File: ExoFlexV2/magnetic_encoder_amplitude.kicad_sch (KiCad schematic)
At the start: 29 parts, among them U11 ADCMP602BRMZ, U12 ADCMP602BRMZ, U13 ADCMP602BRMZ, U14 SN74LVC3G14DCUT_V2, U15 SN74LV4T08PWR_V2, U16 SN74HC7032D_V2, U4 SN74HC7032D_V2

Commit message: quque truc
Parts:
- added C20, C21, C22, C23, C24, C25: 1nF, Capacitor_SMD:C_0603_1608Metric, symbol Device:C
- added R11, R12, R14, R17, R18, R19: 7,5k, Resistor_SMD:R_0603_1608Metric, symbol Device:R_Small_US
- added R13: 150, Resistor_SMD:R_0603_1608Metric, symbol Device:R_Small_US
- added TP10, TP11, TP15, TP6, TP7, TP8, TP9: 5005, FootPrint:KEYSTONE_5005, symbol SymLib:5005
- R10, R8, R9: value R_Small_US -> 5k
- R15: renamed from R11; value R_Small_US -> 3,6k
- R16: renamed from R12; value R_Small_US -> 2,5k
- R7: value R_Small_US -> 2,5k
- renumbered C20 to C26, C21 to C27, C22 to C28, C23 to C29, C24 to C30, C25 to C31, C26 to C32, C27 to C33, C28 to C34, C29 to C35, C30 to C36, C31 to C37, C32 to C38, TP1 to TP12, TP2 to TP13, TP3 to TP14, U11 to U12, U12 to U13, U13 to U14, U14 to U15, U15 to U16, U16 to U17, U4 to U5
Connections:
- net +5V: no longer R15.1, R7.1, R9.1
- net +5VA: now also R7.1, R9.1, R13.1; no longer C26.2, C27.2, C28.2, C29.2, C30.2, C31.2, C32.2, C33.2, C34.2, C35.2, C36.2, C37.2, C38.2, R10.1, R16.1, R8.1, U12.6 (GND), U13.6 (GND), U14.6 (GND), U17.7 (GND)
- net MAG1_POT_OUT: now also R17.1; no longer U12.3 (VN)
- net MAG2_POT_OUT: now also R18.1; no longer U13.3 (VN)
- net MAG3_POT_OUT: now also R19.1; no longer U14.2 (VP), U14.3 (VN)
- net MAG_AMP_1: now also C22.1, R14.2, TP7.TP
- net MAG_AMP_2: now also C21.1, R12.2, TP9.TP
- net MAG_AMP_SEC: now also TP15.TP
- new net: R13.2, R15.1
- new net GND: C20.2, C21.2, C22.2, C23.2, C24.2, C25.2, C26.2, C27.2, C28.2, C29.2, C30.2, C31.2, C32.2, C33.2, C34.2, C35.2, C36.2, C37.2, C38.2, R10.1, R16.1, R8.1, U12.6 (GND), U13.6 (GND), U14.6 (GND), U17.7 (GND)
- new net MAG_AMP_3: C20.1, C25.1, R11.2, R19.2, TP11.TP, TP6.TP, U14.2 (VP), U14.3 (VN)
- new net MAG_LIM_1: C23.1, R17.2, TP8.TP, U12.3 (VN)
- new net MAG_LIM_2: C24.1, R18.2, TP10.TP, U13.3 (VN)
- new net MAG_OUT_1: R14.1
- new net MAG_OUT_2: R12.1
- new net MAG_OUT_3: R11.1
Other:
- moved on the sheet: R10, R15, R16, R7, R8, R9

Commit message: Placement
Début du placement et modification d'après dernier review
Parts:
- added TP29, TP30, TP31: 5005, FootPrint:KEYSTONE_5005, symbol SymLib:5005
- renumbered C22 to C20, C23 to C21, C21 to C22, C24 to C23, C20 to C24, R9 to R10, R10 to R11, R13 to R12, R15 to R13, R16 to R14, R14 to R15, R17 to R16, R12 to R17, R11 to R19, R19 to R20, R7 to R8, R8 to R9, TP7 to TP20, TP8 to TP21, TP9 to TP22, TP10 to TP23, TP6 to TP24, TP11 to TP25, TP12 to TP26, TP13 to TP27, TP14 to TP28, TP15 to TP32, U12 to U10, U13 to U11, U14 to U12, U15 to U13, U5 to U14, U16 to U15, U17 to U16
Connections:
- net MAG_AMP_3: no longer C25.1, R20.2, TP25.TP, U12.3 (VN)
- net at U14.11 (4Y), U16.1 (1A): now also TP30.TP
- net at U15.6 (2Y), U16.2 (1B): now also TP31.TP
- net at U13.5 (2Y), U15.4 (2A): now also TP29.TP
- new net MAG_LIM_3: C25.1, R20.2, TP25.TP, U12.3 (VN)
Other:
- moved on the sheet: C20, C22, C24, C25, R13, R14, R15, R17, R19, R20, TP24, TP26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

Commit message: Placement encore
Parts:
- renumbered C20 to C21, C21 to C22, C22 to C23, C23 to C24, C24 to C25, C25 to C26, C26 to C27, C27 to C28, C28 to C29, C29 to C30, C30 to C31, C31 to C32, C32 to C33, C33 to C34, C34 to C35, C35 to C36, C36 to C37, C37 to C38, C38 to C39, R9 to R10, R10 to R11, R11 to R12, R12 to R13, R13 to R14, R14 to R15, R15 to R16, R16 to R17, R17 to R18, R18 to R19, R19 to R20, R20 to R21, R8 to R9, U10 to U11, U11 to U12, U12 to U13, U13 to U14, U14 to U15, U15 to U16, U16 to U17

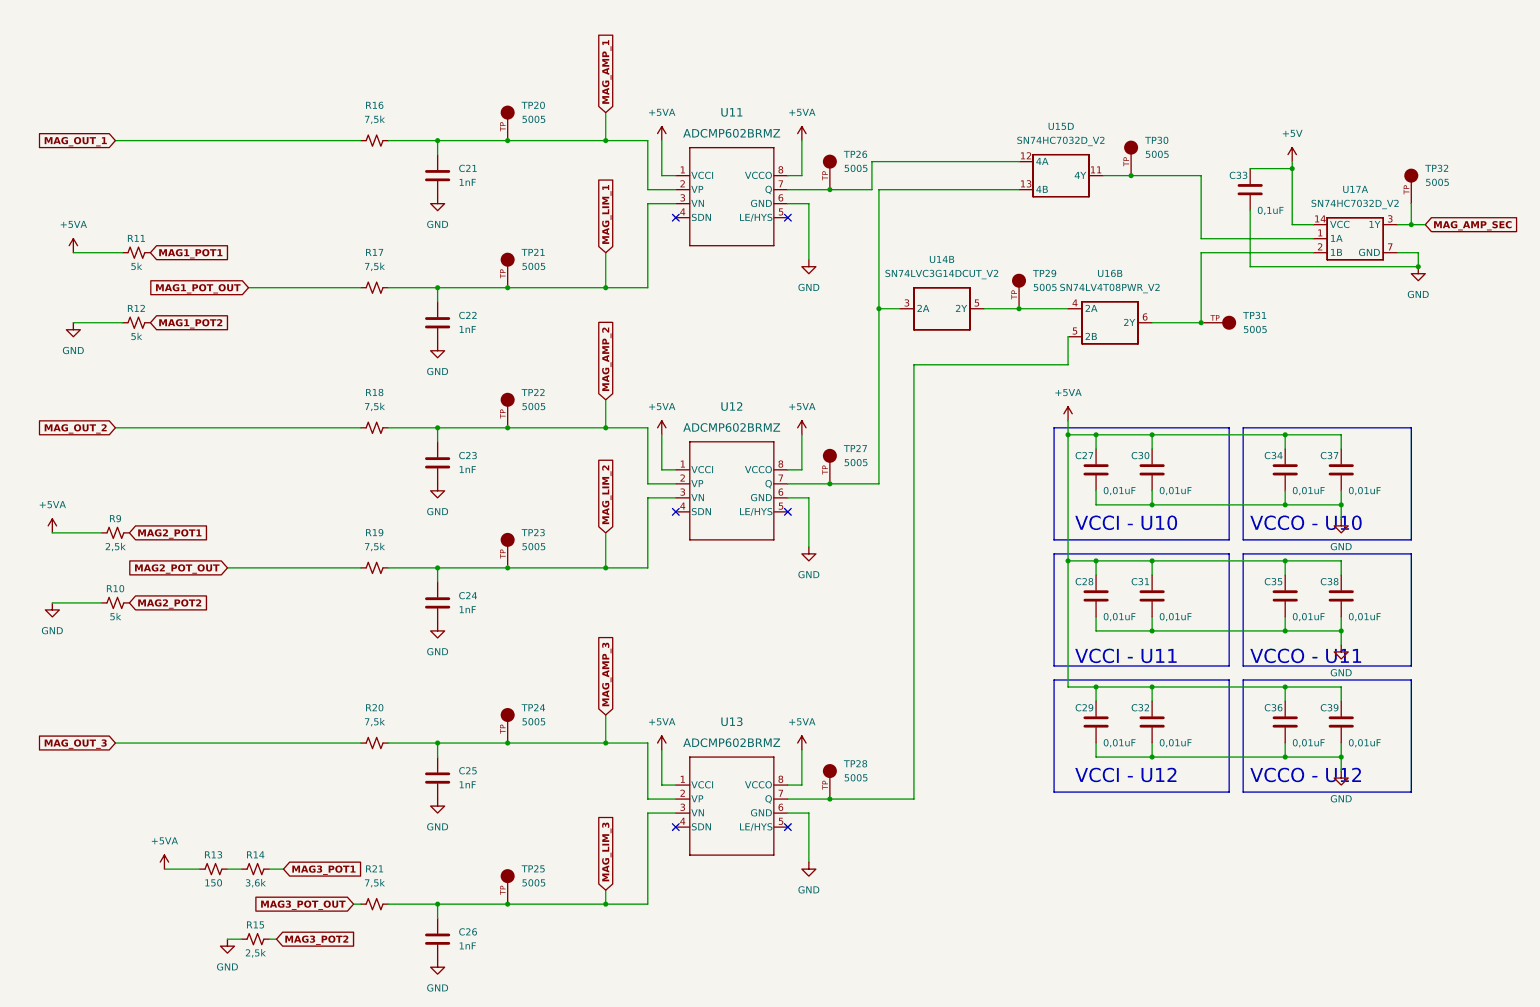
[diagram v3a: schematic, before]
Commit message: Mise à jour mi-stage
- Torque et Amplitude testé et vérifié
- Capteur de présence et de proximité testé
- Système de détection de coupure de fils
- Polyvalence pour plusieurs capteurs
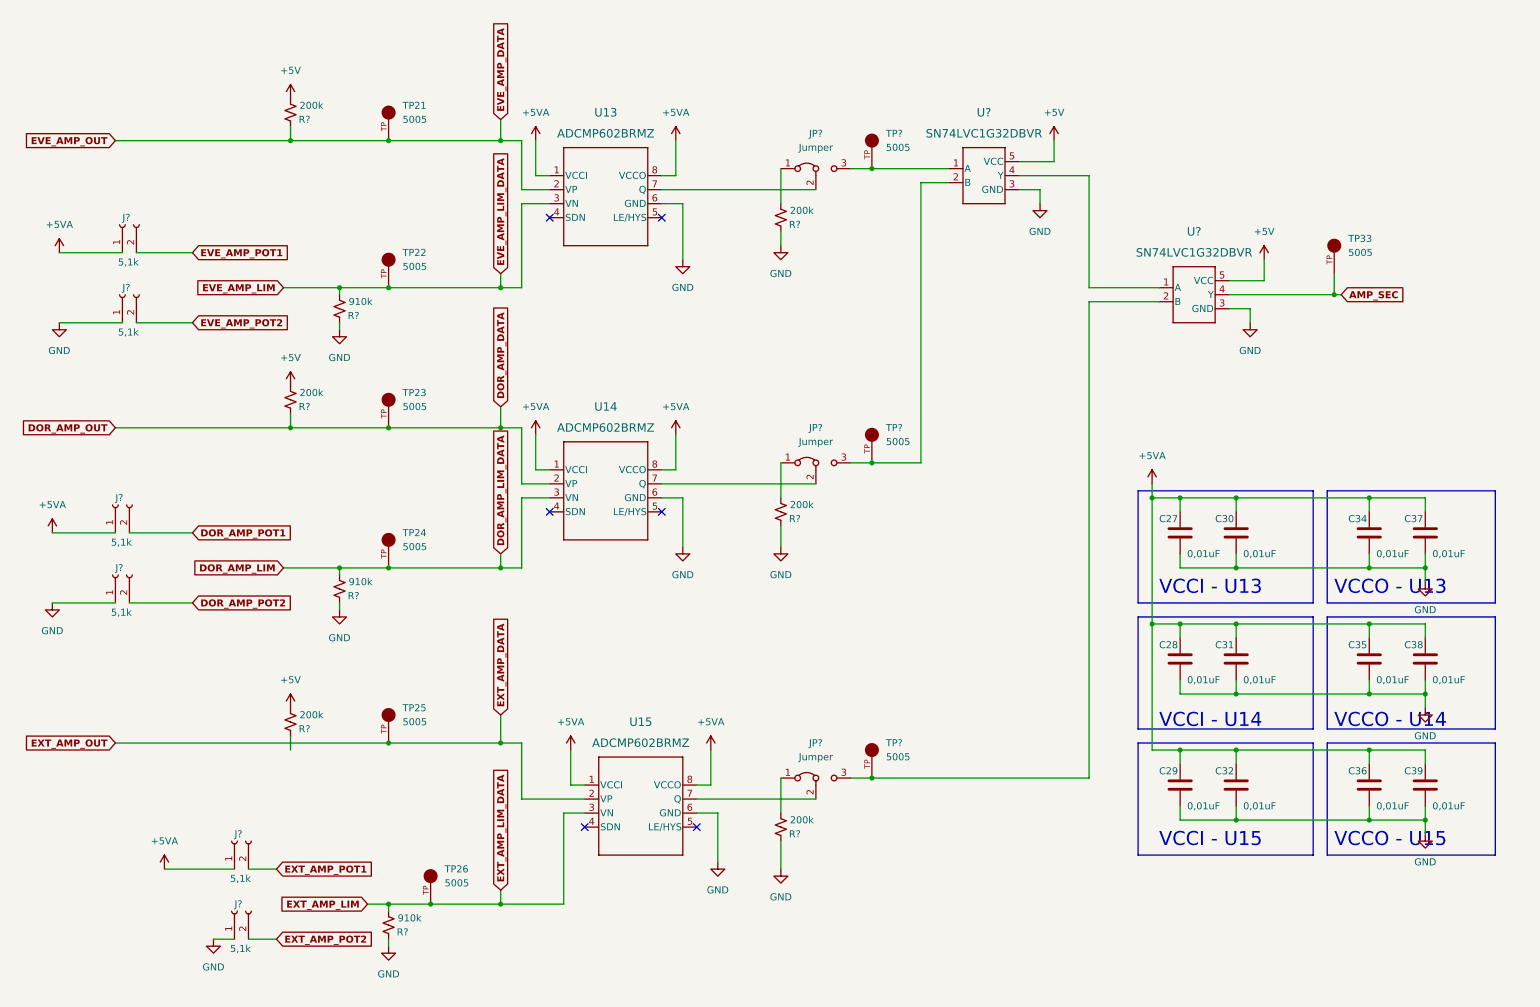
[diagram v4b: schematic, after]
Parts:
- removed C21, C22, C23, C24, C25, C26: 1nF, Capacitor_SMD:C_0603_1608Metric, symbol Device:C
- removed C33: 0,1uF, Capacitor_SMD:C_0603_1608Metric, symbol Device:C
- removed R10, R11, R12: 5k, Resistor_SMD:R_0603_1608Metric, symbol Device:R_Small_US
- removed R13: 150, Resistor_SMD:R_0603_1608Metric, symbol Device:R_Small_US
- removed R14: 3,6k, Resistor_SMD:R_0603_1608Metric, symbol Device:R_Small_US
- removed R15, R9: 2,5k, Resistor_SMD:R_0603_1608Metric, symbol Device:R_Small_US
- removed R16, R17, R18, R19, R20, R21: 7,5k, Resistor_SMD:R_0603_1608Metric, symbol Device:R_Small_US
- removed TP26, TP27, TP28, TP29, TP30, TP31: 5005, FootPrint:KEYSTONE_5005, symbol SymLib:5005
- removed U14: SN74LVC3G14DCUT_V2, FootPrint:SN74LVC3G14DCUT, symbol SymLib:SN74LVC3G14DCUT_V2
- removed U15, U17: SN74HC7032D_V2, FootPrint:SN74HC7032D, symbol SymLib:SN74HC7032D_V2
- removed U16: SN74LV4T08PWR_V2, FootPrint:SN74LV4T08PWR, symbol SymLib:SN74LV4T08PWR_V2
- added J? (x6): 5,1k, Connector_PinHeader_2.54mm:PinHeader_1x02_P2.54mm_Vertical, symbol Connector:Conn_01x02_Female
- added JP? (x3): Jumper, Connector_PinHeader_2.54mm:PinHeader_1x03_P2.54mm_Vertical, symbol Jumper:Jumper_3_Bridged12
- added R? (x3): 910k, Resistor_SMD:R_0603_1608Metric, symbol Device:R_Small_US
- added R? (x6): 200k, Resistor_SMD:R_0603_1608Metric, symbol Device:R_Small_US
- added TP? (x3): 5005, FootPrint:KEYSTONE_5005, symbol SymLib:5005
- added U? (x2): SN74LVC1G32DBVR, FootPrint:SOT95P270X145-5N, symbol SymLib:SN74LVC1G32DBVR
- renumbered TP20 to TP21, TP21 to TP22, TP22 to TP23, TP23 to TP24, TP24 to TP25, TP25 to TP26, TP32 to TP33, U11 to U13, U12 to U14, U13 to U15
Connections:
- net +5V: now also R?.1, R?.1, R?.1, U?.5 (VCC), U?.5 (VCC)
- net +5VA: now also J?.1 (Pin_1), J?.1 (Pin_1), J?.1 (Pin_1)
- net GND: now also J?.1 (Pin_1), J?.1 (Pin_1), J?.1 (Pin_1), R?.2, R?.2, R?.2, R?.2, R?.2, R?.2, U?.3 (GND), U?.3 (GND)
- net at U13.7 (Q): now also JP?.2 (C)
- net at U14.7 (Q): now also JP?.2 (C)
- net at U15.7 (Q): now also JP?.2 (C)
- net MAG_AMP_1 renamed EVE_AMP_DATA
- net EVE_AMP_DATA: now also R?.2
- net MAG_AMP_2 renamed DOR_AMP_DATA
- net DOR_AMP_DATA: now also R?.2
- net MAG_AMP_3 renamed EXT_AMP_DATA
- net MAG_AMP_SEC renamed AMP_SEC
- net AMP_SEC: now also U?.4 (Y)
- net MAG_LIM_1 renamed EVE_AMP_LIM
- net EVE_AMP_LIM: now also R?.1
- net MAG_LIM_2 renamed DOR_AMP_LIM
- net DOR_AMP_LIM: now also R?.1
- net MAG_LIM_3 renamed EXT_AMP_LIM
- net EXT_AMP_LIM: now also R?.1
- new net: U?.1 (A), U?.4 (Y)
- new net: JP?.3 (B), TP?.TP, U?.2 (B) (x2)
- new net: JP?.1 (A), R?.1 (x3)
- new net: JP?.3 (B), TP?.TP, U?.1 (A)
- new net DOR_AMP_POT1: J?.2 (Pin_2)
- new net DOR_AMP_POT2: J?.2 (Pin_2)
- new net EVE_AMP_POT1: J?.2 (Pin_2)
- new net EVE_AMP_POT2: J?.2 (Pin_2)
- new net EXT_AMP_POT1: J?.2 (Pin_2)
- new net EXT_AMP_POT2: J?.2 (Pin_2)
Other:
- note added: "VCCI - U13"
- note added: "VCCI - U14"
- note added: "VCCI - U15"
- note added: "VCCO - U13"
- note added: "VCCO - U14"
- note added: "VCCO - U15"
- note removed: "VCCI - U10"
- note removed: "VCCI - U11"
- note removed: "VCCI - U12"
- note removed: "VCCO - U10"
- note removed: "VCCO - U11"
- note removed: "VCCO - U12"
- moved on the sheet: C27, C28, C29, C30, C31, C32, C34, C35, C36, C37, C38, C39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

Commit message: Mise à jour signaux STM
- Condo de découplage
- Signaux supplémentaire pour le STM
- Page GND sera pour Multiplexeur
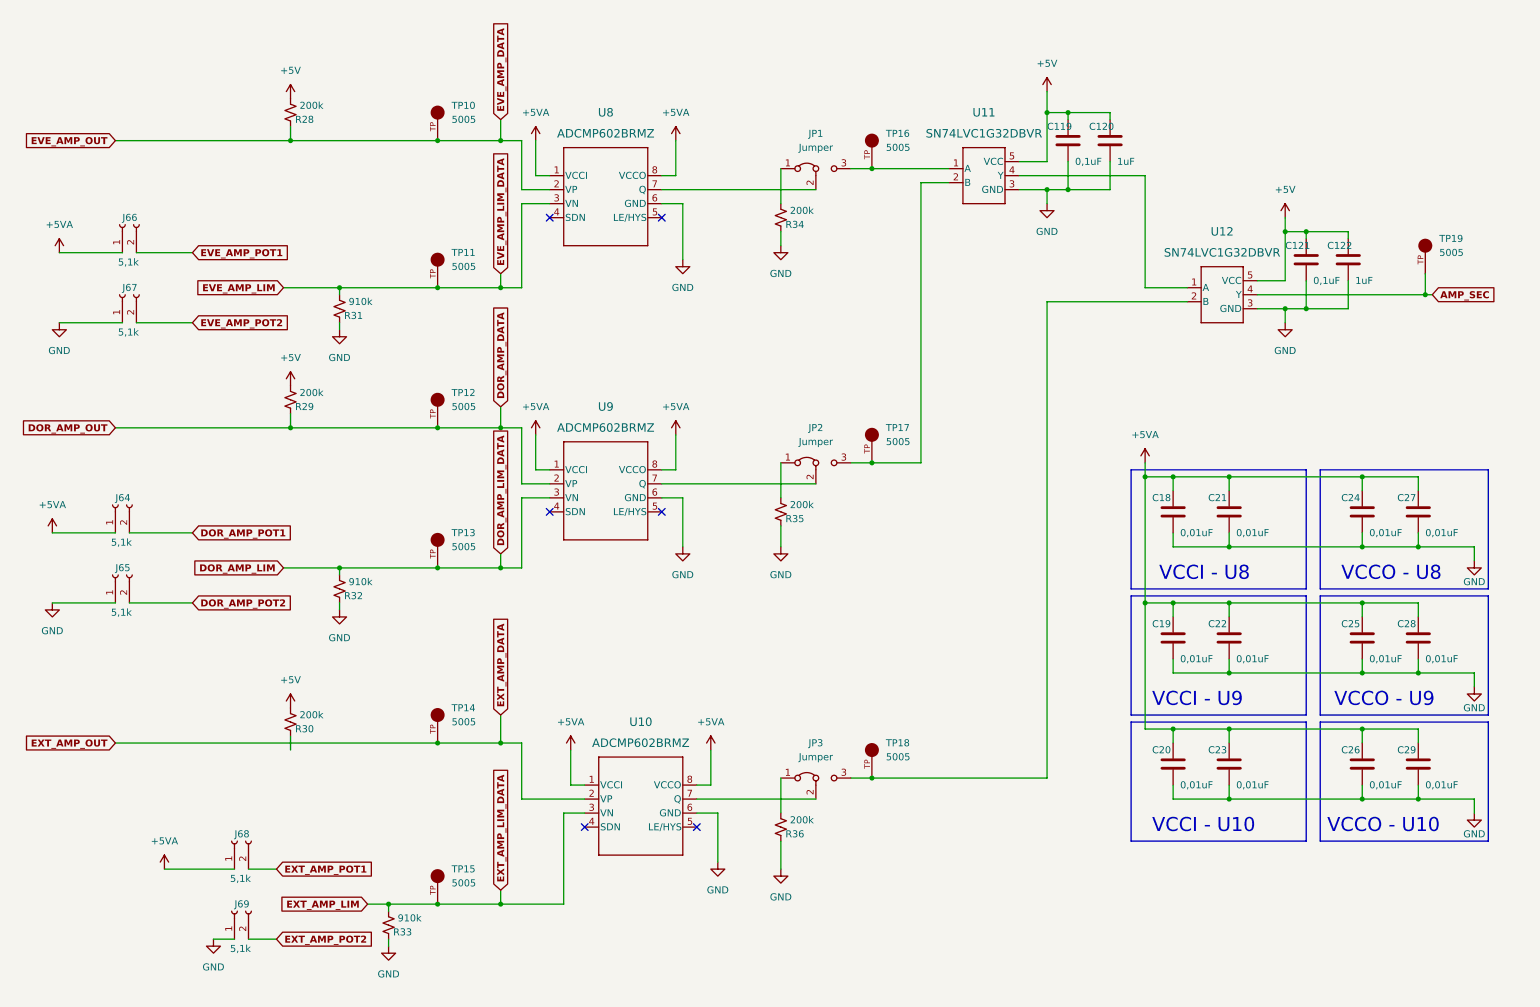
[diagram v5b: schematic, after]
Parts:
- added C119, C121: 0,1uF, Capacitor_SMD:C_0603_1608Metric, symbol Device:C
- added C120, C122: 1uF, Capacitor_SMD:C_0603_1608Metric, symbol Device:C
- gave numbers to parts that had none: 23
- renumbered C27 to C18, C28 to C19, C29 to C20, C30 to C21, C31 to C22, C32 to C23, C34 to C24, C35 to C25, C36 to C26, C37 to C27, C38 to C28, C39 to C29, TP21 to TP10, TP22 to TP11, TP23 to TP12, TP24 to TP13, TP25 to TP14, TP26 to TP15, TP33 to TP19, U15 to U10, U13 to U8, U14 to U9
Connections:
- net +5V: now also C119.1, C120.1, C121.1, C122.1
- net GND: now also C119.2, C120.2, C121.2, C122.2
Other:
- note added: "VCCI - U10"
- note added: "VCCI - U8"
- note added: "VCCI - U9"
- note added: "VCCO - U10"
- note added: "VCCO - U8"
- note added: "VCCO - U9"
- note removed: "VCCI - U13"
- note removed: "VCCI - U14"
- note removed: "VCCI - U15"
- note removed: "VCCO - U13"
- note removed: "VCCO - U14"
- note removed: "VCCO - U15"
- moved on the sheet: C18, C19, C20, C21, C22, C23, C24, C25, C26, C27, C28, C29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

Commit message: Finalisation 1
- Ajout de pages pour la gestion des signaux négatif
- Modification des pages de torque et amplitude
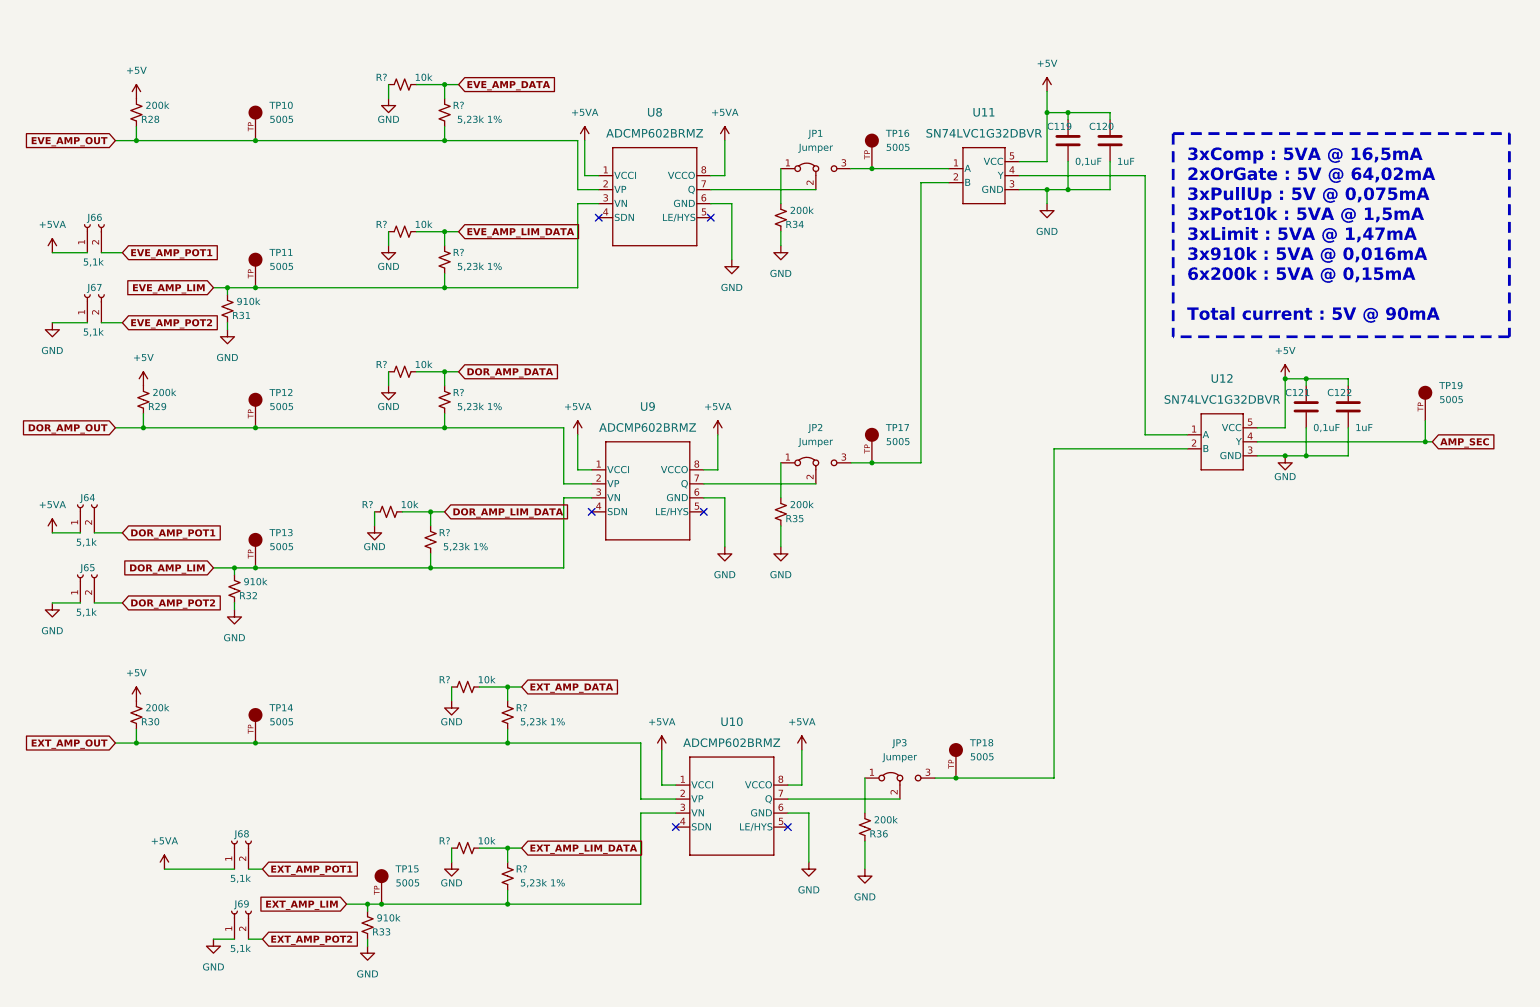
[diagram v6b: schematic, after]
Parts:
- removed C18, C19, C20, C21, C22, C23, C24, C25, C26, C27, C28, C29: 0,01uF, Capacitor_SMD:C_0603_1608Metric, symbol Device:C
- added R? (x6): 5,23k 1%, Resistor_SMD:R_0805_2012Metric, symbol Device:R_Small_US
- added R? (x6): 10k, Resistor_SMD:R_0805_2012Metric, symbol Device:R_Small_US
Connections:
- net DOR_AMP_DATA: now also R?.1, R?.2; no longer R29.2, TP12.TP, U9.2 (VP)
- net DOR_AMP_LIM: now also R?.2
- net EVE_AMP_DATA: now also R?.1, R?.2; no longer R28.2, TP10.TP, U8.2 (VP)
- net EVE_AMP_LIM: now also R?.2
- net EXT_AMP_DATA: now also R?.1, R?.2; no longer TP14.TP, U10.2 (VP)
- net EXT_AMP_LIM: now also R?.2
- net GND: now also R?.1, R?.1, R?.1, R?.1, R?.1, R?.1
- net EXT_AMP_OUT: now reaches R30.2
- net EXT_AMP_OUT: now also TP14.TP, U10.2 (VP), R?.2
- new net DOR_AMP_LIM_DATA: R?.1, R?.2
- new net DOR_AMP_OUT: R29.2, R?.2, TP12.TP, U9.2 (VP)
- new net EVE_AMP_LIM_DATA: R?.1, R?.2
- new net EVE_AMP_OUT: R28.2, R?.2, TP10.TP, U8.2 (VP)
- new net EXT_AMP_LIM_DATA: R?.1, R?.2
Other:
- note added: "3xComp : 5VA @ 16,5mA 2xOrGate : 5V @ 64,02mA 3xPullUp : 5V @ 0,075mA 3xPot10k : 5VA @ 1,5mA 3xLimit : 5VA @ 1,47mA 3x910k : 5VA @ 0,016mA 6x200k : 5VA @ 0,15mA Total current : 5V @ 90mA"
- note removed: "VCCI - U10"
- note removed: "VCCI - U8"
- note removed: "VCCI - U9"
- note removed: "VCCO - U10"
- note removed: "VCCO - U8"
- note removed: "VCCO - U9"
- moved on the sheet: C121, C122, J64, J65, J66, J67, JP3, R28, R29, R30, R31, R32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
